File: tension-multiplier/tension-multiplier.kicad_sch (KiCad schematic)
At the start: 4 parts, among them J1 Conn_01x03_Pin, J2 Conn_01x02_Pin, J3 Conn_01x02_Pin, U1 AD633ANZ

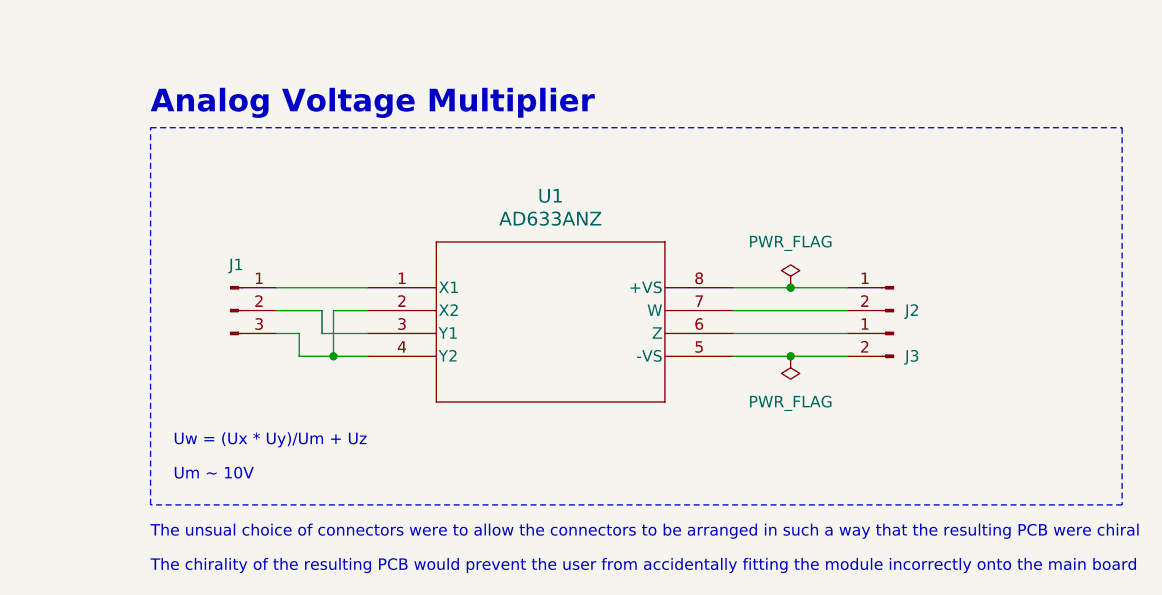
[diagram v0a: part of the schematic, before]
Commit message: Starts PCB layout for analog multiplier
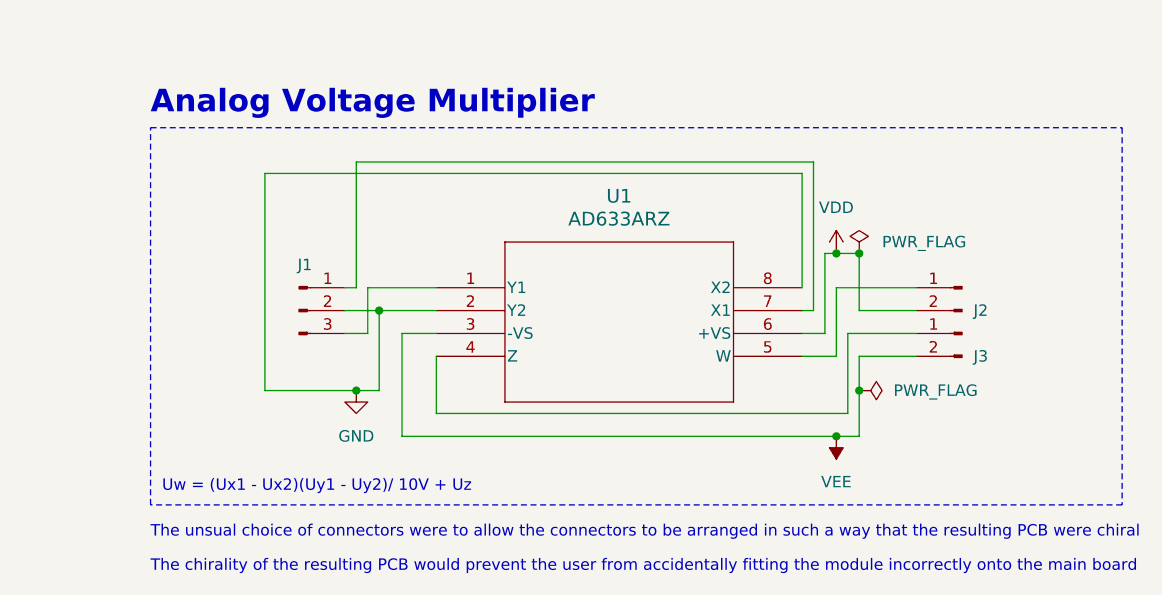
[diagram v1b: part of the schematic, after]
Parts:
- removed U1: AD633ANZ, footprints:N_8_ADI, symbol 2024-01-23_03-22-31:AD633ANZ
- added U1: AD633ARZ, R_8_ADI, symbol 2024-02-06_17-08-26:AD633ARZ
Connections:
- net at J3.1 (Pin_1): now also U1.4 (Z)
- net VEE: now reaches J3.2 (Pin_2)
- net VEE: now also U1.3 (-VS)
- net at J2.1 (Pin_1): now also U1.5 (W)
- net VDD: now reaches J2.2 (Pin_2)
- net VDD: now also U1.6 (+VS)
- net at J1.1 (Pin_1): now also U1.7 (X1)
- net at J1.3 (Pin_3): now also U1.1 (Y1)
- net GND: now reaches J1.2 (Pin_2)
- net GND: now also U1.2 (Y2), U1.8 (X2)
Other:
- note added: "Uw = (Ux1 - Ux2)(Uy1 - Uy2)/ 10V + Uz"
- note removed: "Um ~ 10V"
- note removed: "Uw = (Ux * Uy)/Um + Uz"
- moved on the sheet: J1, J2, J3

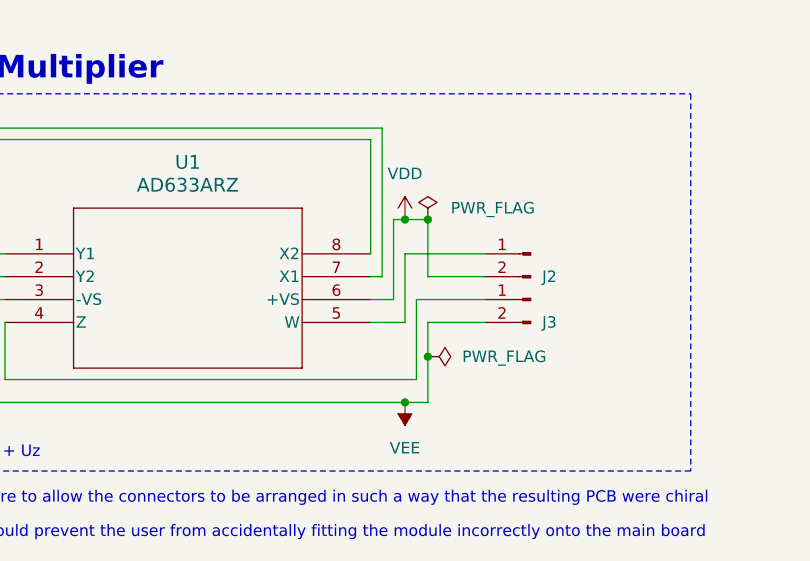
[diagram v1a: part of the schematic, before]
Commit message: Modifies auxiliary boards
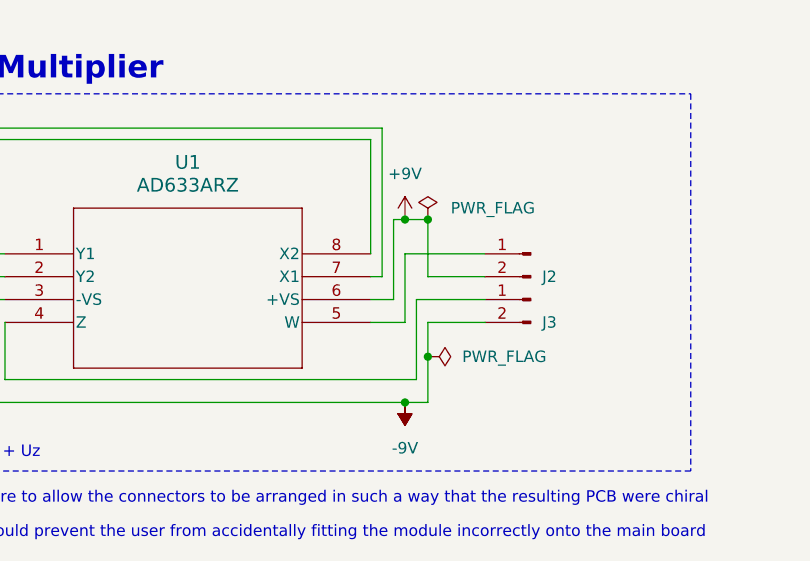
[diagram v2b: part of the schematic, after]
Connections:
- net VDD renamed +9V
- net VEE renamed -9V
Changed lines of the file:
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@@
   (junction (at 172.72 96.52) (diameter 0) (color 0 0 0 0)
   )
+  (junction (at 170.18 81.28) (diameter 0) (color 0 0 0 0)
+  )
   (junction (at 116.84 96.52) (diameter 0) (color 0 0 0 0)
   )
@@
   (junction (at 170.18 101.6) (diameter 0) (color 0 0 0 0)
   )
-  (junction (at 170.18 81.28) (diameter 0) (color 0 0 0 0)
+  (wire (pts (xy 170.18 81.28) (xy 172.72 81.28))
+    (stroke (width 0) (type default))
   )
   (wire (pts (xy 166.37 92.71) (xy 170.18 92.71))
@@
     (stroke (width 0) (type default))
   )
+  (wire (pts (xy 121.92 101.6) (xy 170.18 101.6))
+    (stroke (width 0) (type default))
+  )
+  (wire (pts (xy 167.64 87.63) (xy 167.64 71.12))
+    (stroke (width 0) (type default))
+  )
+  (wire (pts (xy 172.72 81.28) (xy 172.72 87.63))
+    (stroke (width 0) (type default))
+  )
+  (wire (pts (xy 172.72 101.6) (xy 172.72 96.52))
+    (stroke (width 0) (type default))
+  )
+  (wire (pts (xy 170.18 85.09) (xy 170.18 92.71))
+    (stroke (width 0) (type default))
+  )
+  (wire (pts (xy 115.57 87.63) (xy 119.38 87.63))
+    (stroke (width 0) (type default))
+  )
+  (wire (pts (xy 125.73 87.63) (xy 119.38 87.63))
+    (stroke (width 0) (type default))
+  )
+  (wire (pts (xy 166.37 90.17) (xy 168.91 90.17))
+    (stroke (width 0) (type default))
+  )
+  (wire (pts (xy 116.84 85.09) (xy 115.57 85.09))
+    (stroke (width 0) (type default))
+  )
+  (polyline (pts (xy 93.98 109.22) (xy 93.98 67.31))
+    (stroke (width 0) (type dash))
+  )
+  (wire (pts (xy 106.68 72.39) (xy 106.68 96.52))
+    (stroke (width 0) (type default))
+  )
+  (wire (pts (xy 166.37 72.39) (xy 106.68 72.39))
+    (stroke (width 0) (type default))
+  )
+  (polyline (pts (xy 201.93 67.31) (xy 201.93 109.22))
+    (stroke (width 0) (type dash))
+  )
+  (polyline (pts (xy 93.98 67.31) (xy 201.93 67.31))
+    (stroke (width 0) (type dash))
+  )
   (wire (pts (xy 168.91 81.28) (xy 170.18 81.28))
-    (stroke (width 0) (type default))
-  )
-  (wire (pts (xy 121.92 101.6) (xy 170.18 101.6))
-    (stroke (width 0) (type default))
-  )
-  (wire (pts (xy 167.64 87.63) (xy 167.64 71.12))
-    (stroke (width 0) (type default))
-  )
-  (wire (pts (xy 172.72 81.28) (xy 172.72 87.63))
-    (stroke (width 0) (type default))
-  )
-  (wire (pts (xy 172.72 101.6) (xy 172.72 96.52))
-    (stroke (width 0) (type default))
-  )
-  (wire (pts (xy 170.18 85.09) (xy 170.18 92.71))
-    (stroke (width 0) (type default))
-  )
-  (wire (pts (xy 115.57 87.63) (xy 119.38 87.63))
-    (stroke (width 0) (type default))
-  )
-  (wire (pts (xy 125.73 87.63) (xy 119.38 87.63))
-    (stroke (width 0) (type default))
-  )
-  (wire (pts (xy 166.37 90.17) (xy 168.91 90.17))
-    (stroke (width 0) (type default))
-  )
-  (wire (pts (xy 116.84 85.09) (xy 115.57 85.09))
-    (stroke (width 0) (type default))
-  )
-  (polyline (pts (xy 93.98 109.22) (xy 93.98 67.31))
-    (stroke (width 0) (type dash))
-  )
-  (wire (pts (xy 106.68 72.39) (xy 106.68 96.52))
-    (stroke (width 0) (type default))
-  )
-  (wire (pts (xy 166.37 72.39) (xy 106.68 72.39))
-    (stroke (width 0) (type default))
-  )
-  (polyline (pts (xy 201.93 67.31) (xy 201.93 109.22))
-    (stroke (width 0) (type dash))
-  )
-  (polyline (pts (xy 93.98 67.31) (xy 201.93 67.31))
-    (stroke (width 0) (type dash))
-  )
-  (wire (pts (xy 170.18 81.28) (xy 172.72 81.28))
     (stroke (width 0) (type default))
   )
@@
   (text "Uw = (Ux1 - Ux2)(Uy1 - Uy2)/ 10V + Uz" (at 95.25 107.95 0)
     (effects (font (size 1.27 1.27)) (justify left bottom))
+  )
+  (symbol (lib_id "power:-9V") (at 170.18 101.6 180) (unit 1)
+    (in_bom yes) (on_board yes) (dnp no) (fields_autoplaced)
+    (property "Reference" "#PWR04" (at 170.18 98.425 0)
+      (effects (font (size 1.27 1.27)) hide)
+    )
+    (property "Value" "-9V" (at 170.18 106.68 0)
+      (effects (font (size 1.27 1.27)))
+    )
+    (property "Footprint" "" (at 170.18 101.6 0)
+      (effects (font (size 1.27 1.27)) hide)
+    )
+    (property "Datasheet" "" (at 170.18 101.6 0)
+      (effects (font (size 1.27 1.27)) hide)
+    )
+    (pin "1")
+    (instances
+      (project "tension-multiplier"
+        (path "/14bea607-1587-48a1-8e26-756968a8898f"
+          (reference "#PWR04") (unit 1)
+        )
+      )
+    )
   )
   (symbol (lib_id "power:GND") (at 116.84 96.52 0) (unit 1)
@@
     )
   )
-  (symbol (lib_id "power:VDD") (at 170.18 81.28 0) (unit 1)
-    (in_bom yes) (on_board yes) (dnp no) (fields_autoplaced)
-    (property "Reference" "#PWR01" (at 170.18 85.09 0)
-      (effects (font (size 1.27 1.27)) hide)
-    )
-    (property "Value" "VDD" (at 170.18 76.2 0)
-      (effects (font (size 1.27 1.27)))
-    )
-    (property "Footprint" "" (at 170.18 81.28 0)
-      (effects (font (size 1.27 1.27)) hide)
-    )
-    (property "Datasheet" "" (at 170.18 81.28 0)
-      (effects (font (size 1.27 1.27)) hide)
-    )
-    (pin "1")
-    (instances
-      (project "tension-multiplier"
-        (path "/14bea607-1587-48a1-8e26-756968a8898f"
-          (reference "#PWR01") (unit 1)
-        )
-      )
-    )
-  )
   (symbol (lib_id "power:VEE") (at 170.18 101.6 180) (unit 1)
     (in_bom yes) (on_board yes) (dnp no) (fields_autoplaced)
@@
     )
     (property "Value" "VEE" (at 170.18 106.68 0)
-      (effects (font (size 1.27 1.27)))
+      (effects (font (size 1.27 1.27)) hide)
     )
     (property "Footprint" "" (at 170.18 101.6 0)
@@
         )
       )
+    )
+  )
+  (symbol (lib_id "power:+9V") (at 170.18 81.28 0) (unit 1)
+    (in_bom yes) (on_board yes) (dnp no) (fields_autoplaced)
+    (property "Reference" "#PWR01" (at 170.18 85.09 0)
+      (effects (font (size 1.27 1.27)) hide)
+    )
+    (property "Value" "+9V" (at 170.18 76.2 0)
+      (effects (font (size 1.27 1.27)))
+    )
+    (property "Footprint" "" (at 170.18 81.28 0)
+      (effects (font (size 1.27 1.27)) hide)
+    )
+    (property "Datasheet" "" (at 170.18 81.28 0)
+      (effects (font (size 1.27 1.27)) hide)
+    )
+    (pin "1")
+    (instances
+      (project "tension-multiplier"
+        (path "/14bea607-1587-48a1-8e26-756968a8898f"
+          (reference "#PWR01") (unit 1)
+        )
+      )
